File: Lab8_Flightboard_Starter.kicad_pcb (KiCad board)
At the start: 2 copper layers, 80 x 80 mm, 64 parts, among them J1 Motor1, J10 ESC3_GND, J11 ESC4_VBAT, J12 ESC4_GND, J2 Motor2, J3 Motor3, J4 Motor4, J5 ESC1_VBAT, J6 ESC1_GND, J7 ESC2_VBAT, J8 ESC2_GND, J9 ESC3_VBAT, Q1 DMP6023LE-13, U1 Teensy4.0, U2 TPS62933, U4 LP5912-3.3DRV, U5 LP5912-3.3DRV, U6 NRF24L01_Breakout, U9 LSM6DSO32_Adafruit

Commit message: Updated wiring
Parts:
- moved D1 14.2 mm to (126.0, 100.5)
- moved C3 7.46 mm to (124.0, 107.5)
- moved D4 5.50 mm to (121.4, 99.5)
- moved R1 5.37 mm to (130.0, 96.0), turned to 180 degrees
- moved C1 5.17 mm to (117.5, 106.0)
- moved C2 5.17 mm to (121.5, 106.1)
- moved D2 4.77 mm to (120.0, 111.5)
- moved C4 1.08 mm to (130.5, 99.5), turned to 0 degrees
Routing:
- net /SYS_VIN: track 32.7 -> 39.9 mm
- net Net-(D4-~-Pad1): track 13.3 -> 19.6 mm, vias 2 -> 4
- net /5V_OUT: track 109.4 -> 105.6 mm
- net Net-(C6-Pad1): track 19.9 -> 22.1 mm
- net Net-(U2-SS): track 4.55 -> 6.48 mm

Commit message: Moved more parts
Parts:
- moved D4 7.30 mm to (123.5, 106.5), turned to 180 degrees
- moved C1 6.04 mm to (120.0, 111.5), turned to 0 degrees
- moved C3 5.70 mm to (119.5, 104.0), turned to 0 degrees
- moved D2 4.03 mm to (119.5, 115.5)
- moved C2 2.88 mm to (119.0, 107.5), turned to 0 degrees
- moved C4 0.50 mm to (130.5, 100.0)
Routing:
- net Net-(D4-~-Pad1): track 19.6 -> 35.0 mm
- net /5V_OUT: track 105.6 -> 103.3 mm
- net /SYS_VIN: track 39.9 -> 42.0 mm
- net Net-(C6-Pad1): track 22.1 -> 20.6 mm
- net Net-(U2-SS): track 6.48 -> 5.98 mm

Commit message: Added bom and gerber
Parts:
- moved BT1 2.64 mm to (111.8, 97.9)
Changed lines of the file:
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@@
 	(footprint "FC_Mechanical:Pad_x2"
 		(layer "F.Cu")
-		(at 112.15 100.525 -90)
+		(at 111.85 97.9 -90)
 		(property "Reference" "BT1"
 			(at 0 -7.5 270)
@@
 			(polygon
 				(pts
-					(xy 115.55 101.825) (xy 115.55 108.025) (xy 109.05 108.025) (xy 109.05 101.825)
+					(xy 115.25 99.2) (xy 115.25 105.4) (xy 108.75 105.4) (xy 108.75 99.2)
 				)
 			)
@@
 			(polygon
 				(pts
-					(xy 115.553308 93.025) (xy 115.553308 99.225) (xy 109.04669 99.225) (xy 109.04669 93.025)
+					(xy 115.253308 90.4) (xy 115.253308 96.6) (xy 108.74669 96.6) (xy 108.74669 90.4)
 				)
 			)
@@
 	)
 	(via
-		(at 112.3 104.925)
+		(at 112 102.3)
 		(size 0.6)
 		(drill 0.3)

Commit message: Updated wiring again
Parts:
- moved U2 1.03 mm to (130.9, 104.5)
- moved C6 0.47 mm to (128.2, 109.5)
- moved BT1 0.25 mm to (112.1, 97.9)
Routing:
- net Net-(U2-BST): track 11.6 -> 5.55 mm
- net Net-(U2-SS): track 5.98 -> 4.96 mm
- net /SYS_VIN: track 42.0 -> 43.0 mm
- net Net-(U2-SW): track 13.5 -> 14.3 mm
- net Net-(C6-Pad1): track 20.6 -> 20.0 mm

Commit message: Remade the power plane + updates
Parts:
- moved R4 5.48 mm to (136.0, 121.5)
- moved C14 4.82 mm to (141.0, 128.0)
- moved C15 4.82 mm to (137.0, 128.0)
- moved C13 3.53 mm to (132.0, 121.5)
- moved R5 2.06 mm to (134.5, 118.0)
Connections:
- R4 pad 2: /VBAT -> /SYS_VIN
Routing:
- net /SYS_VIN: track 43.0 -> 63.3 mm, vias 0 -> 2
- net /VBAT: track 33.3 -> 27.7 mm, vias 2 -> 0
- net /5V_OUT: track 103.3 -> 99.3 mm
- net Net-(D4-~-Pad1): track 35.0 -> 33.2 mm, vias 4 -> 6

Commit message: Edited some dimensions
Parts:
- moved J10 0.12 mm to (111.4, 134.0)
- moved J9 0.12 mm to (118.8, 134.0)
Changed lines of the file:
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@@
 	(footprint "FC_Mechanical:Pad_x1_6mm"
 		(layer "F.Cu")
-		(at 111.431698 133.875 180)
+		(at 111.431698 134 180)
 		(property "Reference" "J10"
 			(at -0.068302 3.875 0)
@@
 			(polygon
 				(pts
-					(xy 114.431698 137.278308) (xy 108.231698 137.278308) (xy 108.231698 130.77169) (xy 114.431698 130.77169)
+					(xy 114.431698 137.403308) (xy 108.231698 137.403308) (xy 108.231698 130.89669) (xy 114.431698 130.89669)
 				)
 			)
@@
 	(footprint "FC_Mechanical:Pad_x1_6mm"
 		(layer "F.Cu")
-		(at 118.75 133.875 180)
+		(at 118.75 134 180)
 		(property "Reference" "J9"
 			(at 0.25 3.875 0)
@@
 			(polygon
 				(pts
-					(xy 121.75 137.278308) (xy 115.55 137.278308) (xy 115.55 130.77169) (xy 121.75 130.77169)
+					(xy 121.75 137.403308) (xy 115.55 137.403308) (xy 115.55 130.89669) (xy 121.75 130.89669)
 				)
 			)
@@
 	)
 	(segment
-		(start 116.5 131.875)
-		(end 118.65 134.025)
+		(start 126.989 103.3432)
+		(end 126 102.3542)
+		(width 0.2)
+		(layer "F.Cu")
+		(net "/SYS_VIN")
+	)
+	(segment
+		(start 117.4375 107.5)
+		(end 117.4375 110.5)
 		(width 0.8)
 		(layer "F.Cu")
-		(net "/VBAT")
+		(net "/SYS_VIN")
 	)
 	(segment
-		(start 118 93.5)
-		(end 112.25 93.5)
-		(width 0.9)
+		(start 118.4625 106.475)
+		(end 117.4375 107.5)
+		(width 0.8)
 		(layer "F.Cu")
-		(net "/VBAT")
+		(net "/SYS_VIN")
 	)
 	(segment
-		(start 121.15 83.325)
-		(end 121.15 84.6)
+		(start 124.965886 103.7)
+		(end 123.727207 103.7)
 		(width 0.8)
 		(layer "F.Cu")
-		(net "/VBAT")
+		(net "/SYS_VIN")
 	)
 	(segment
-		(start 121.15 89.725)
-		(end 121.15 90.35)
-		(width 0.9)
+		(start 128.3958 104.75)
+		(end 126 102.3542)
+		(width 0.2)
 		(layer "F.Cu")
-		(net "/VBAT")
+		(net "/SYS_VIN")
 	)
 	(segment
-		(start 121.15 84.6)
-		(end 112.25 93.5)
+		(start 118.4625 104)
+		(end 118.4625 106.475)
 		(width 0.8)
 		(layer "F.Cu")
-		(net "/VBAT")
+		(net "/SYS_VIN")
 	)
 	(segment
-		(start 121.15 90.35)
-		(end 118 93.5)
-		(width 0.9)
+		(start 130.16 104.75)
+		(end 128.3958 104.75)
+		(width 0.2)
 		(layer "F.Cu")
-		(net "/VBAT")
+		(net "/SYS_VIN")
+	)
+	(segment
+		(start 118.4625 104)
+		(end 120.4625 106)
+		(width 0.8)
+		(layer "F.Cu")
+		(net "/SYS_VIN")
+	)
+	(segment
+		(start 137 121.5)
+		(end 137 120)
+		(width 0.2)
+		(layer "F.Cu")
+		(net "/SYS_VIN")
+	)
+	(segment
+		(start 123.45 89.725)
+		(end 121.595 91.58)
+		(width 0.8)
+		(layer "F.Cu")
+		(net "/SYS_VIN")
+	)
+	(segment
+		(start 117.4375 110.5)
+		(end 118.4375 111.5)
+		(width 0.8)
+		(layer "F.Cu")
+		(net "/SYS_VIN")
+	)
+	(segment
+		(start 126 102.3542)
+		(end 126 102.665886)
+		(width 0.8)
+		(layer "F.Cu")
+		(net "/SYS_VIN")
+	)
+	(segment
+		(start 123.727207 103.7)
+		(end 122.9 102.872793)
+		(width 0.8)
+		(layer "F.Cu")
+		(net "/SYS_VIN")
+	)
+	(segment
+		(start 126 102.665886)
+		(end 124.965886 103.7)
+		(width 0.8)
+		(layer "F.Cu")
+		(net "/SYS_VIN")
+	)
+	(segment
+		(start 122.9 102.127207)
+		(end 121.640293 100.8675)
+		(width 0.8)
+		(layer "F.Cu")
+		(net "/SYS_VIN")
+	)
+	(segment
+		(start 120.4625 106)
+		(end 121.94 106)
+		(width 0.8)
+		(layer "F.Cu")
+		(net "/SYS_VIN")
+	)
+	(segment
+		(start 121.94 106)
+		(end 122.44 106.5)
+		(width 0.8)
+		(layer "F.Cu")
+		(net "/SYS_VIN")
+	)
+	(segment
+		(start 121.595 91.58)
+		(end 121.595 100.8675)
+		(width 0.8)
+		(layer "F.Cu")
+		(net "/SYS_VIN")
+	)
+	(segment
+		(start 121.640293 100.8675)
+		(end 121.595 100.8675)
+		(width 0.8)
+		(layer "F.Cu")
+		(net "/SYS_VIN")
+	)
+	(segment
+		(start 122.9 102.872793)
+		(end 122.9 102.127207)
+		(width 0.8)
+		(layer "F.Cu")
+		(net "/SYS_VIN")
+	)
+	(segment
+		(start 121.595 100.8675)
+		(end 118.4625 104)
+		(width 0.8)
+		(layer "F.Cu")
+		(net "/SYS_VIN")
+	)
+	(via
+		(at 128.3958 104.75)
+		(size 0.6)
+		(drill 0.3)
+		(layers "F.Cu" "B.Cu")
+		(net "/SYS_VIN")
+	)
+	(via
+		(at 137 120)
+		(size 0.6)
+		(drill 0.3)
+		(layers "F.Cu" "B.Cu")
+		(net "/SYS_VIN")
+	)
+	(segment
+		(start 128.3958 111.3958)
+		(end 128.3958 104.75)
+		(width 0.2)
+		(layer "B.Cu")
+		(net "/SYS_VIN")
+	)
+	(segment
+		(start 137 120)
+		(end 128.3958 111.3958)
+		(width 0.2)
+		(layer "B.Cu")
+		(net "/SYS_VIN")
 	)
 	(segment
@@
 	)
 	(segment
-		(start 126.989 103.3432)
-		(end 126 102.3542)
-		(width 0.2)
-		(layer "F.Cu")
-		(net "/SYS_VIN")
-	)
-	(segment
-		(start 117.4375 107.5)
-		(end 117.4375 110.5)
-		(width 0.8)
-		(layer "F.Cu")
-		(net "/SYS_VIN")
-	)
-	(segment
-		(start 118.4625 106.475)
-		(end 117.4375 107.5)
-		(width 0.8)
-		(layer "F.Cu")
-		(net "/SYS_VIN")
-	)
-	(segment
-		(start 124.965886 103.7)
-		(end 123.727207 103.7)
-		(width 0.8)
-		(layer "F.Cu")
-		(net "/SYS_VIN")
-	)
-	(segment
-		(start 128.3958 104.75)
-		(end 126 102.3542)
-		(width 0.2)
-		(layer "F.Cu")
-		(net "/SYS_VIN")
-	)
-	(segment
-		(start 118.4625 104)
-		(end 118.4625 106.475)
-		(width 0.8)
-		(layer "F.Cu")
-		(net "/SYS_VIN")
-	)
-	(segment
-		(start 130.16 104.75)
-		(end 128.3958 104.75)
-		(width 0.2)
-		(layer "F.Cu")
-		(net "/SYS_VIN")
-	)
-	(segment
-		(start 118.4625 104)
-		(end 120.4625 106)
-		(width 0.8)
-		(layer "F.Cu")
-		(net "/SYS_VIN")
-	)
-	(segment
-		(start 137 121.5)
-		(end 137 120)
-		(width 0.2)
-		(layer "F.Cu")
-		(net "/SYS_VIN")
-	)
-	(segment
-		(start 123.45 89.725)
-		(end 121.595 91.58)
-		(width 0.8)
-		(layer "F.Cu")
-		(net "/SYS_VIN")
-	)
-	(segment
-		(start 117.4375 110.5)
-		(end 118.4375 111.5)
-		(width 0.8)
-		(layer "F.Cu")
-		(net "/SYS_VIN")
-	)
-	(segment
-		(start 126 102.3542)
-		(end 126 102.665886)
-		(width 0.8)
-		(layer "F.Cu")
-		(net "/SYS_VIN")
-	)
-	(segment
-		(start 123.727207 103.7)
-		(end 122.9 102.872793)
-		(width 0.8)
-		(layer "F.Cu")
-		(net "/SYS_VIN")
-	)
-	(segment
-		(start 126 102.665886)
-		(end 124.965886 103.7)
-		(width 0.8)
-		(layer "F.Cu")
-		(net "/SYS_VIN")
-	)
-	(segment
-		(start 122.9 102.127207)
-		(end 121.640293 100.8675)
-		(width 0.8)
-		(layer "F.Cu")
-		(net "/SYS_VIN")
-	)
-	(segment
-		(start 120.4625 106)
-		(end 121.94 106)
-		(width 0.8)
-		(layer "F.Cu")
-		(net "/SYS_VIN")
-	)
-	(segment
-		(start 121.94 106)
-		(end 122.44 106.5)
-		(width 0.8)
-		(layer "F.Cu")
-		(net "/SYS_VIN")
-	)
-	(segment
-		(start 121.595 91.58)
-		(end 121.595 100.8675)
-		(width 0.8)
-		(layer "F.Cu")
-		(net "/SYS_VIN")
-	)
-	(segment
-		(start 121.640293 100.8675)
-		(end 121.595 100.8675)
-		(width 0.8)
-		(layer "F.Cu")
-		(net "/SYS_VIN")
-	)
-	(segment
-		(start 122.9 102.872793)
-		(end 122.9 102.127207)
-		(width 0.8)
-		(layer "F.Cu")
-		(net "/SYS_VIN")
-	)
-	(segment
-		(start 121.595 100.8675)
-		(end 118.4625 104)
-		(width 0.8)
-		(layer "F.Cu")
-		(net "/SYS_VIN")
-	)
-	(via
-		(at 128.3958 104.75)
-		(size 0.6)
-		(drill 0.3)
-		(layers "F.Cu" "B.Cu")
-		(net "/SYS_VIN")
-	)
-	(via
-		(at 137 120)
-		(size 0.6)
-		(drill 0.3)
-		(layers "F.Cu" "B.Cu")
-		(net "/SYS_VIN")
-	)
-	(segment
-		(start 128.3958 111.3958)
-		(end 128.3958 104.75)
-		(width 0.2)
-		(layer "B.Cu")
-		(net "/SYS_VIN")
-	)
-	(segment
-		(start 137 120)
-		(end 128.3958 111.3958)
-		(width 0.2)
-		(layer "B.Cu")
-		(net "/SYS_VIN")
-	)
-	(segment
 		(start 168.65 76.65)
 		(end 168.65 73.025)
@@
 	)
 	(segment
+		(start 116.5 131.875)
+		(end 118.65 134.025)
+		(width 0.8)
+		(layer "F.Cu")
+		(net "/VBAT")
+	)
+	(segment
+		(start 118 93.5)
+		(end 112.25 93.5)
+		(width 0.9)
+		(layer "F.Cu")
+		(net "/VBAT")
+	)
+	(segment
+		(start 121.15 83.325)
+		(end 121.15 84.6)
+		(width 0.8)
+		(layer "F.Cu")
+		(net "/VBAT")
+	)
+	(segment
+		(start 121.15 89.725)
+		(end 121.15 90.35)
+		(width 0.9)
+		(layer "F.Cu")
+		(net "/VBAT")
+	)
+	(segment
+		(start 121.15 84.6)
+		(end 112.25 93.5)
+		(width 0.8)
+		(layer "F.Cu")
+		(net "/VBAT")
+	)
+	(segment
+		(start 121.15 90.35)
+		(end 118 93.5)
+		(width 0.9)
+		(layer "F.Cu")
+		(net "/VBAT")
+	)
+	(segment
 		(start 122 104)
 		(end 122 102.5)
@@
 		(polygon
 			(pts
-				(xy 107 59.5) (xy 108 58.5) (xy 186 58.5) (xy 187 60) (xy 187 66.5) (xy 116 66.5) (xy 116 130.24468)
-				(xy 187 130.748226) (xy 187 137.5) (xy 186 138.5) (xy 108 138.5) (xy 107 137.5)
+				(xy 107 59.5) (xy 108 58.5) (xy 186 58.5) (xy 187 60) (xy 187 67) (xy 116 67) (xy 116 130.5) (xy 187 130.5)
+				(xy 187 137.5) (xy 186 138.5) (xy 108 138.5) (xy 107 137.5)
 			)
 		)

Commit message: Improved the design
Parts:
- R10, R12, R6, R8: value 47 -> 100k
- R11, R13, R7, R9: value 100k -> 47
- moved D4 11.0 mm to (133.0, 101.0)
- moved C5 9.00 mm to (126.5, 105.0), turned to 90 degrees
- moved U2 7.52 mm to (124.0, 107.5)
- moved C4 7.21 mm to (124.5, 104.0), turned to -90 degrees
- moved R3 6.61 mm to (136.0, 104.5), turned to 0 degrees
- moved R2 3.96 mm to (131.5, 105.5), turned to 0 degrees
- moved C11 1.75 mm to (163.5, 90.5)
- moved C9 1.70 mm to (165.5, 111.0)
- moved C2 1.41 mm to (120.0, 106.5), turned to 180 degrees
- moved C12 1.38 mm to (171.0, 90.5)
- moved C1 1.30 mm to (119.5, 110.3), turned to 180 degrees
- moved D1 1.12 mm to (125.5, 99.5), turned to 180 degrees
- moved C25 1.07 mm to (170.5, 85.0)
- moved R6 1.03 mm to (123.7, 77.5)
- moved R8 1.03 mm to (171.7, 78.0)
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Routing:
- net Net-(U2-FB): track 12.5 -> 19.0 mm
- net Net-(D4-~-Pad1): track 33.2 -> 26.8 mm, vias 6 -> 4
- net /SYS_VIN: track 63.3 -> 69.3 mm, vias 2 -> 3
- net Net-(C6-Pad1): track 20.0 -> 15.6 mm
- net Net-(U2-SW): track 14.3 -> 18.0 mm
- net /5V_OUT: track 99.3 -> 103.0 mm
- net Net-(U2-BST): track 5.55 -> 3.29 mm
- net Net-(U2-SS): track 4.96 -> 3.03 mm
- net /MOTOR2: track 9.83 -> 8.41 mm
- net GND: track 4.72 -> 3.50 mm
- net /3.3V_IMU: track 49.2 -> 48.6 mm
- net /3.3V_GP: track 41.3 -> 40.7 mm
- net /MOTOR3: track 7.68 -> 8.25 mm

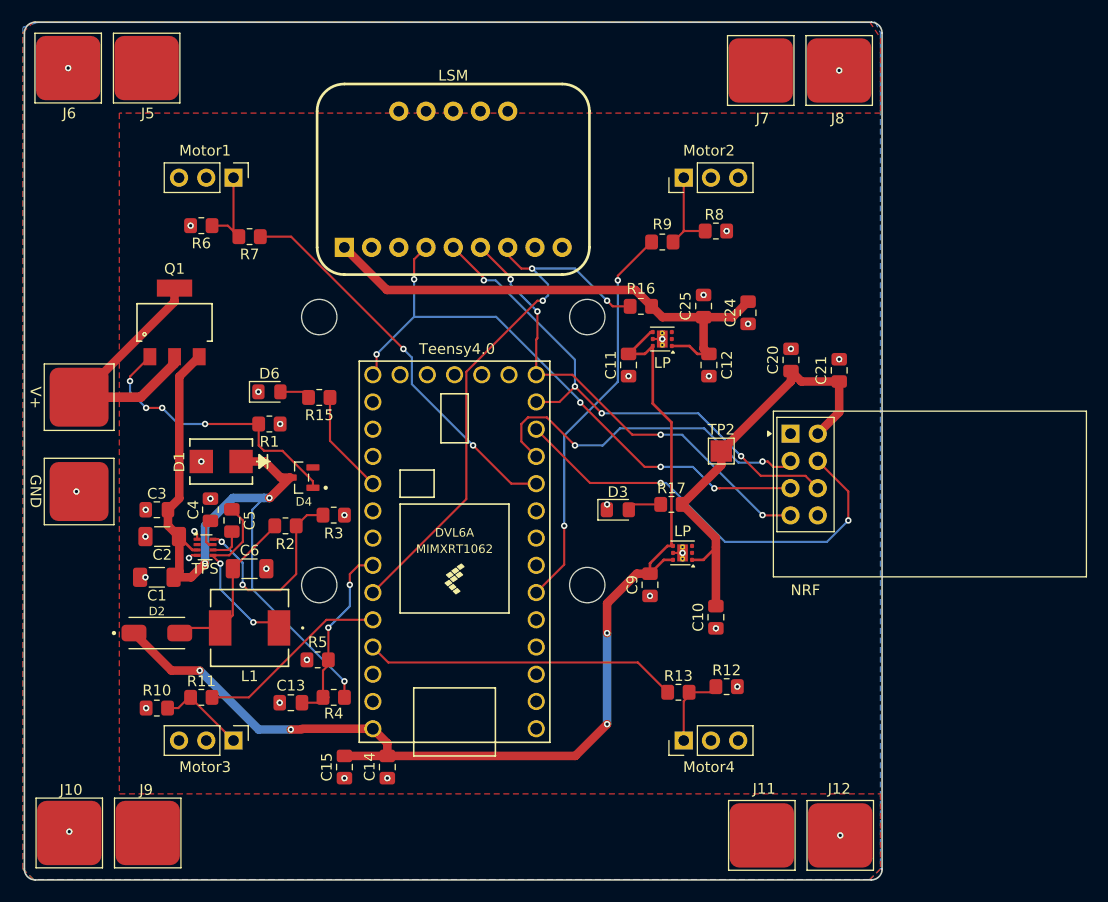
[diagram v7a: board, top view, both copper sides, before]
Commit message: Added 4x4 array for ground vias
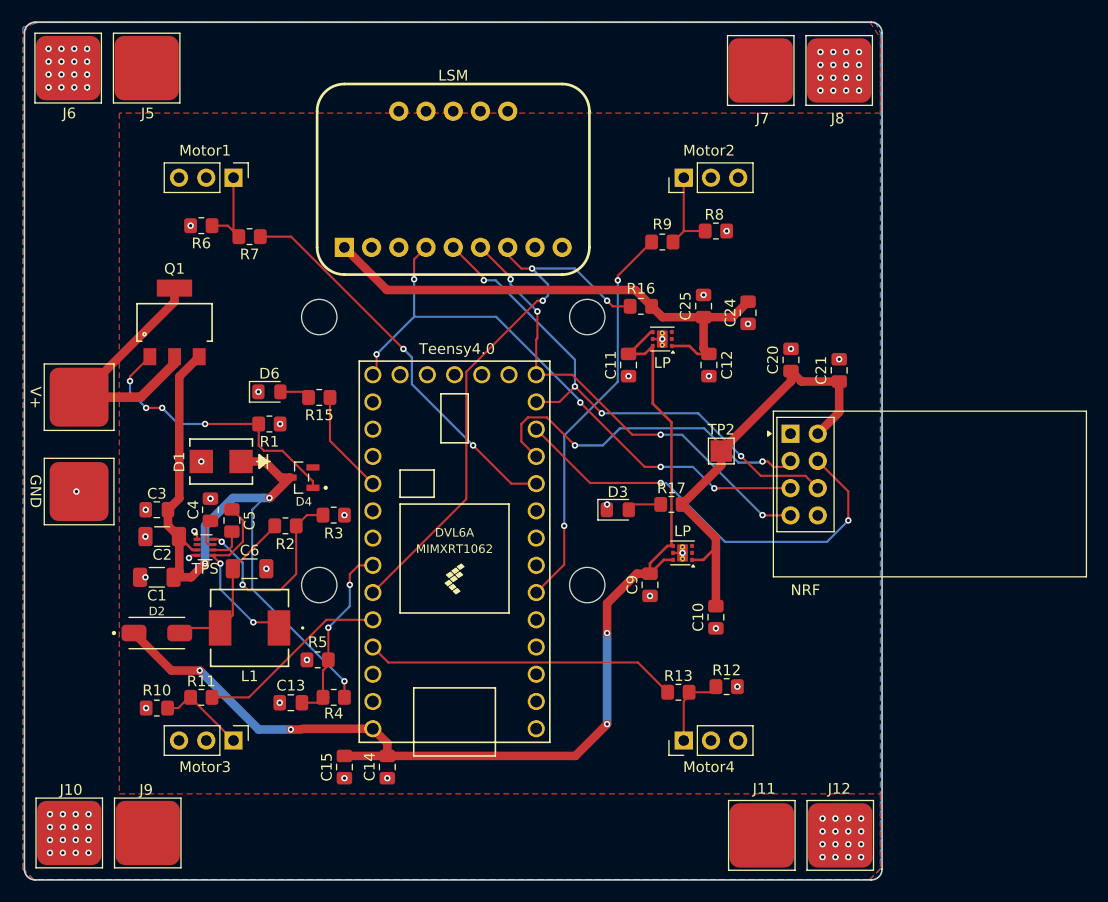
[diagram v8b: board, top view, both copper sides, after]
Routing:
- net GND: vias 35 -> 95
